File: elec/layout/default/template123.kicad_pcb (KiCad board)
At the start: 2 copper layers, 40 x 40 mm, 0 parts

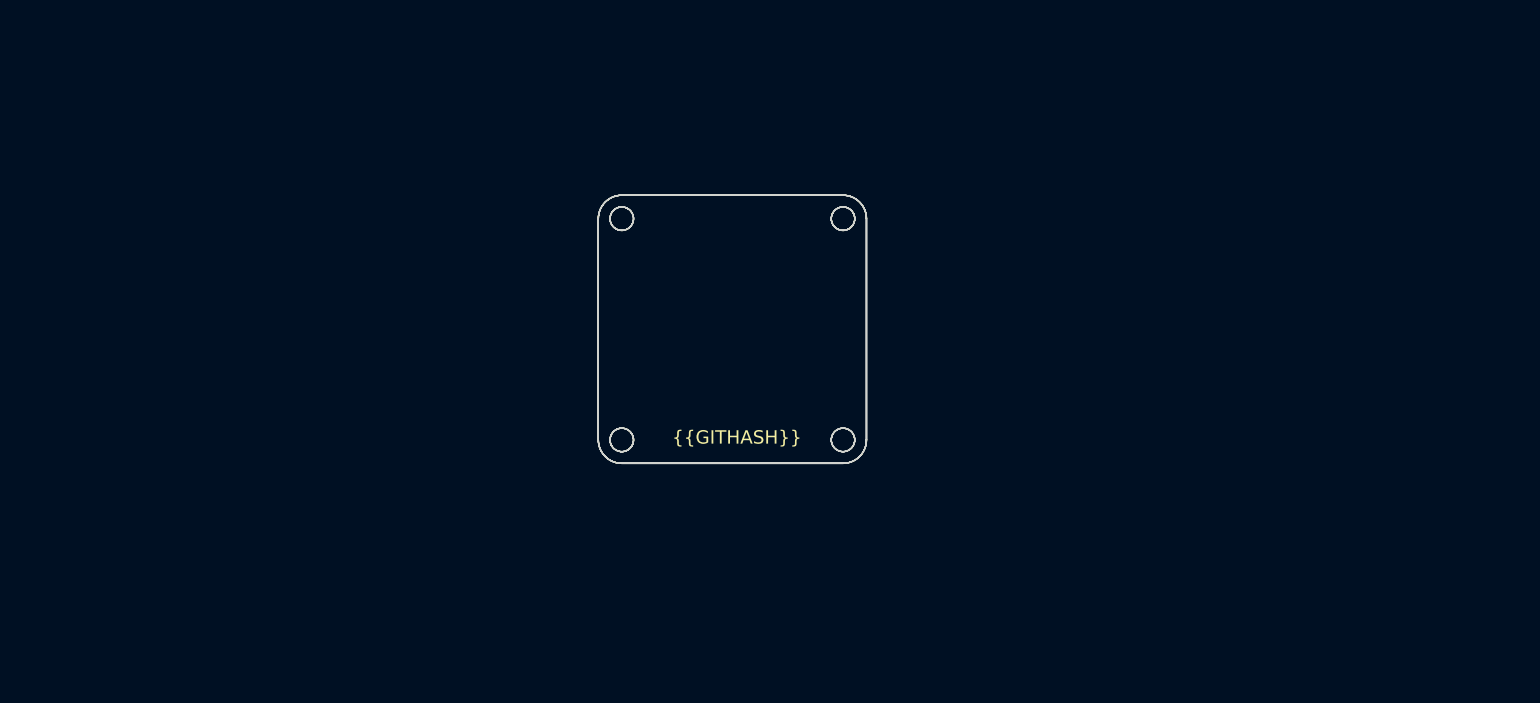
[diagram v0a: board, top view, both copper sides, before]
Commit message: added holiday themeed board shapes
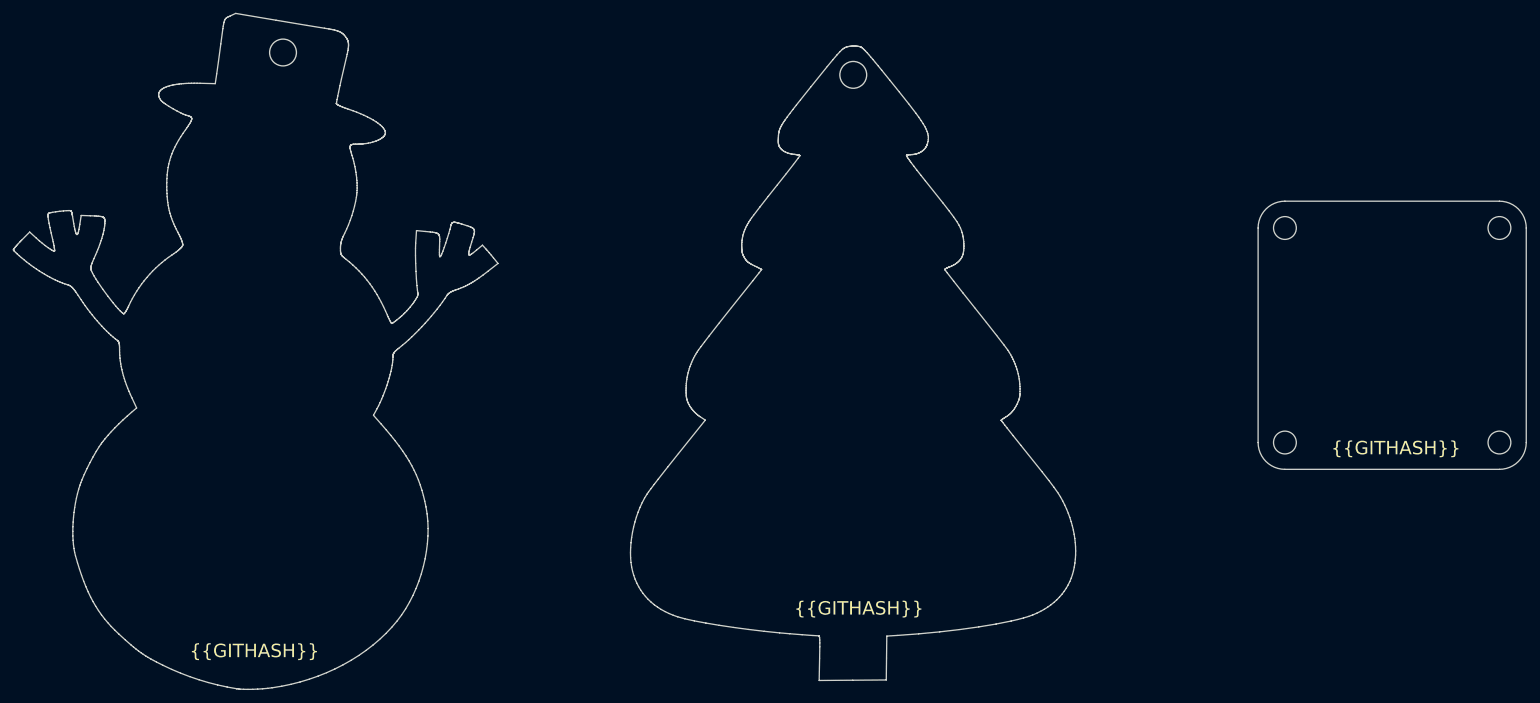
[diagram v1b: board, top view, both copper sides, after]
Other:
- board size 40 x 40 mm -> 225.7 x 100.8 mm
